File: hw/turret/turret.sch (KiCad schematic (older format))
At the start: 13 parts, among them M1 Motor_Servo wingturn, M2 Motor_Servo wingspan, Q1 MJE3055, SW1 SW_Push, U1 ESP-WROOM-32module, U2 GY291module, U3 AM312module

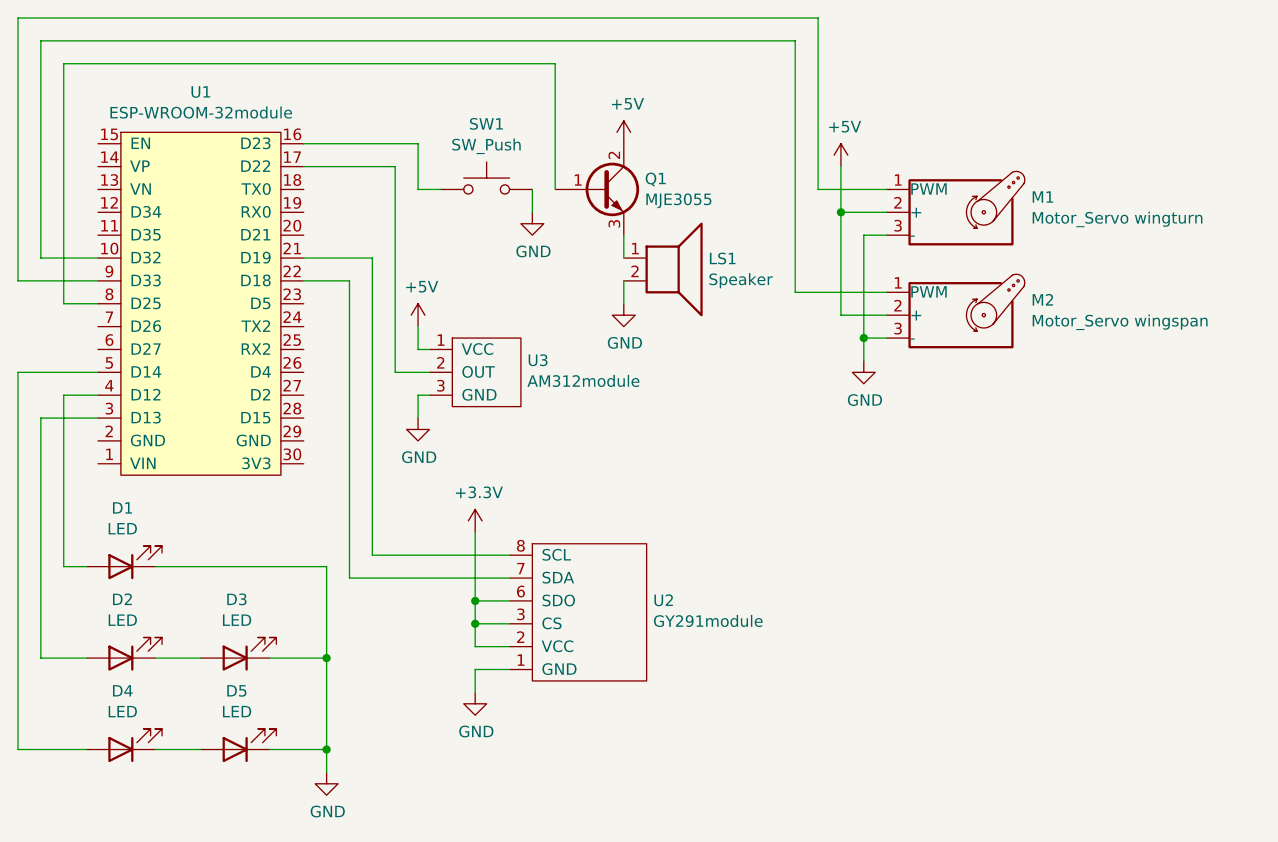
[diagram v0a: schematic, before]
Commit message: hw: adjust schematics for v2 and add PCB
Signed-off-by: Max Filippov <jcmvbkbc@gmail.com>
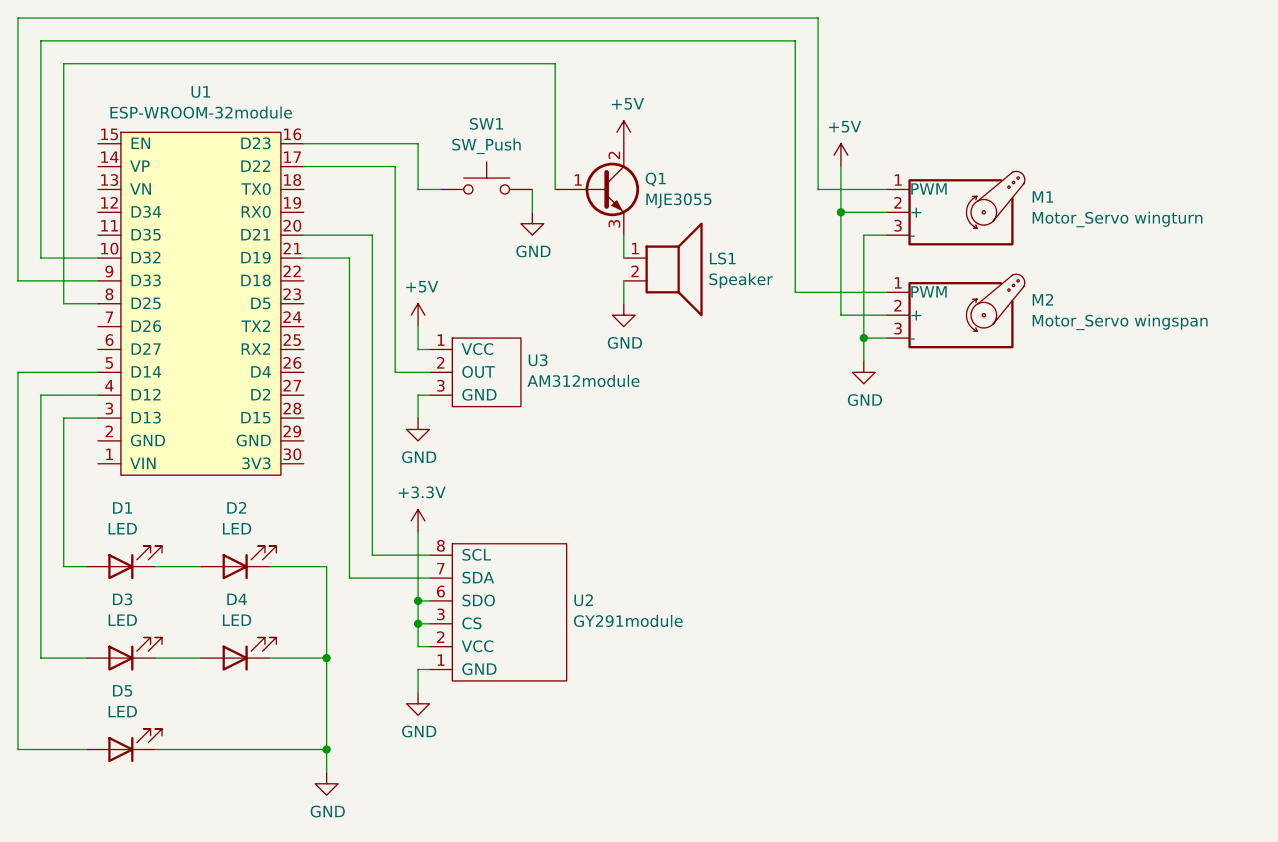
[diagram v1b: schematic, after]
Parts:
- renumbered D2 to D1, D3 to D2, D4 to D3, D5 to D4, D1 to D5
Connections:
- net at U2.7 (SDA): now also U1.21 (D19); no longer U1.22 (D18)
- net at U2.8 (SCL): now also U1.20 (D21); no longer U1.21 (D19)
- net at U1.4 (D12): now also D3.2 (A); no longer D5.2 (A)
- net at U1.5 (D14): now also D5.2 (A); no longer D3.2 (A)
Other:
- moved on the sheet: D1, D2, D3, D4, D5, U2
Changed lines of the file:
@@
 EELAYER 30 0
 EELAYER END
-$Descr A4 11693 8268
+$Descr USLetter 8500 11000 portrait
 encoding utf-8
 Sheet 1 1
-Title ""
-Date ""
-Rev ""
+Title "Portal Turret"
+Date "2023-04-10"
+Rev "v2"
 Comp ""
 Comment1 ""
@@
 Connection ~ 5200 1900
 Wire Wire Line
-	1950 2700 1800 2700
-Wire Wire Line
-	1950 2800 1700 2800
-Wire Wire Line
-	1950 2600 1600 2600
+	1950 2800 1800 2800
 Wire Wire Line
 	1800 2300 1950 2300
@@
 L helpers:GY291module U2
 U 1 1 64208805
-P 4100 3650
-F 0 "U2" H 4378 3701 50  0000 L CNN
-F 1 "GY291module" H 4378 3610 50  0000 L CNN
-F 2 "" H 4100 3700 50  0001 C CNN
-F 3 "" H 4100 3700 50  0001 C CNN
-	1    4100 3650
-	1    0    0    -1
-$EndComp
-Wire Wire Line
-	3050 2200 2850 2200
-Wire Wire Line
-	3150 2100 2850 2100
+P 3750 3650
+F 0 "U2" H 4028 3701 50  0000 L CNN
+F 1 "GY291module" H 4028 3610 50  0000 L CNN
+F 2 "" H 3750 3700 50  0001 C CNN
+F 3 "" H 3750 3700 50  0001 C CNN
+	1    3750 3650
+	1    0    0    -1
+$EndComp
 $Comp
 L power:+3.3V #PWR?
 U 1 1 6420E29C
-P 3600 3300
-F 0 "#PWR?" H 3600 3150 50  0001 C CNN
-F 1 "+3.3V" H 3615 3473 50  0000 C CNN
-F 2 "" H 3600 3300 50  0001 C CNN
-F 3 "" H 3600 3300 50  0001 C CNN
-	1    3600 3300
-	1    0    0    -1
-$EndComp
-Wire Wire Line
-	3750 3800 3600 3800
-Wire Wire Line
-	3600 3800 3600 3700
-Wire Wire Line
-	3750 3700 3600 3700
-Connection ~ 3600 3700
+P 3350 3300
+F 0 "#PWR?" H 3350 3150 50  0001 C CNN
+F 1 "+3.3V" H 3365 3473 50  0000 C CNN
+F 2 "" H 3350 3300 50  0001 C CNN
+F 3 "" H 3350 3300 50  0001 C CNN
+	1    3350 3300
+	1    0    0    -1
+$EndComp
+Wire Wire Line
+	3400 3800 3350 3800
+Wire Wire Line
+	3350 3800 3350 3700
+Wire Wire Line
+	3400 3700 3350 3700
+Connection ~ 3350 3700
 $Comp
 L power:GND #PWR?
 U 1 1 64210F0B
-P 3600 4000
-F 0 "#PWR?" H 3600 3750 50  0001 C CNN
-F 1 "GND" H 3605 3827 50  0000 C CNN
-F 2 "" H 3600 4000 50  0001 C CNN
-F 3 "" H 3600 4000 50  0001 C CNN
-	1    3600 4000
-	1    0    0    -1
-$EndComp
-Wire Wire Line
-	3750 3900 3600 3900
+P 3350 4000
+F 0 "#PWR?" H 3350 3750 50  0001 C CNN
+F 1 "GND" H 3355 3827 50  0000 C CNN
+F 2 "" H 3350 4000 50  0001 C CNN
+F 3 "" H 3350 4000 50  0001 C CNN
+	1    3350 4000
+	1    0    0    -1
+$EndComp
+Wire Wire Line
+	3400 3900 3350 3900
 $Comp
 L helpers:AM312module U3
@@
 	1600 1050 1600 2200
 Wire Wire Line
-	1600 2600 1600 4250
-Wire Wire Line
-	1700 2800 1700 3850
-Wire Wire Line
-	1800 3450 1900 3450
-Wire Wire Line
-	1800 2700 1800 3450
-Wire Wire Line
-	1900 4250 1600 4250
+	1800 2800 1800 3450
 Wire Wire Line
 	1900 3850 1700 3850
 Connection ~ 2950 3850
 Wire Wire Line
+	2950 3450 2700 3450
+Wire Wire Line
 	2950 3850 2950 3450
-Connection ~ 2950 4250
 Wire Wire Line
 	2950 3850 2700 3850
-Wire Wire Line
-	2950 4250 2950 3850
-Wire Wire Line
-	2950 4250 2700 4250
 Wire Wire Line
 	2950 4350 2950 4250
@@
 $EndComp
 Wire Wire Line
-	2200 4250 2400 4250
-Wire Wire Line
 	2200 3850 2400 3850
-$Comp
-L Device:LED D5
+Wire Wire Line
+	2200 3450 2400 3450
+$Comp
+L Device:LED D4
 U 1 1 642176FC
-P 2550 4250
-F 0 "D5" H 2543 3995 50  0000 C CNN
-F 1 "LED" H 2543 4086 50  0000 C CNN
-F 2 "" H 2550 4250 50  0001 C CNN
-F 3 "~" H 2550 4250 50  0001 C CNN
-	1    2550 4250
-	-1   0    0    1
-$EndComp
-$Comp
-L Device:LED D4
-U 1 1 64217295
-P 2050 4250
-F 0 "D4" H 2043 3995 50  0000 C CNN
-F 1 "LED" H 2043 4086 50  0000 C CNN
-F 2 "" H 2050 4250 50  0001 C CNN
-F 3 "~" H 2050 4250 50  0001 C CNN
-	1    2050 4250
-	-1   0    0    1
-$EndComp
-$Comp
-L Device:LED D3
-U 1 1 64216CAC
 P 2550 3850
-F 0 "D3" H 2543 3595 50  0000 C CNN
+F 0 "D4" H 2543 3595 50  0000 C CNN
 F 1 "LED" H 2543 3686 50  0000 C CNN
 F 2 "" H 2550 3850 50  0001 C CNN
@@
 $EndComp
 $Comp
-L Device:LED D2
-U 1 1 64215029
+L Device:LED D3
+U 1 1 64217295
 P 2050 3850
-F 0 "D2" H 2043 3595 50  0000 C CNN
+F 0 "D3" H 2043 3595 50  0000 C CNN
 F 1 "LED" H 2043 3686 50  0000 C CNN
 F 2 "" H 2050 3850 50  0001 C CNN
@@
 $EndComp
 $Comp
+L Device:LED D2
+U 1 1 64216CAC
+P 2550 3450
+F 0 "D2" H 2543 3195 50  0000 C CNN
+F 1 "LED" H 2543 3286 50  0000 C CNN
+F 2 "" H 2550 3450 50  0001 C CNN
+F 3 "~" H 2550 3450 50  0001 C CNN
+	1    2550 3450
+	-1   0    0    1
+$EndComp
+$Comp
 L Device:LED D1
-U 1 1 64212CAF
+U 1 1 64215029
 P 2050 3450
 F 0 "D1" H 2043 3195 50  0000 C CNN
@@
 	-1   0    0    1
 $EndComp
+$Comp
+L Device:LED D5
+U 1 1 64212CAF
+P 2050 4250
+F 0 "D5" H 2043 3995 50  0000 C CNN
+F 1 "LED" H 2043 4086 50  0000 C CNN
+F 2 "" H 2050 4250 50  0001 C CNN
+F 3 "~" H 2050 4250 50  0001 C CNN
+	1    2050 4250
+	-1   0    0    1
+$EndComp
 Wire Wire Line
 	3950 1800 3950 1250
@@
 	1700 2100 1700 1150
 Wire Wire Line
-	3600 3300 3600 3600
-Wire Wire Line
-	3750 3600 3600 3600
-Wire Wire Line
-	3600 3900 3600 4000
-Wire Wire Line
-	2950 3450 2200 3450
-Wire Wire Line
-	3150 2100 3150 3400
-Wire Wire Line
-	3150 3400 3750 3400
-Wire Wire Line
-	3050 2200 3050 3500
-Wire Wire Line
-	3050 3500 3750 3500
-Connection ~ 3600 3600
-Wire Wire Line
-	3600 3600 3600 3700
+	3350 3300 3350 3600
+Wire Wire Line
+	3400 3600 3350 3600
+Wire Wire Line
+	3350 3900 3350 4000
+Wire Wire Line
+	3150 3400 3400 3400
+Wire Wire Line
+	3050 3500 3400 3500
+Connection ~ 3350 3600
+Wire Wire Line
+	3350 3600 3350 3700
+Wire Wire Line
+	2850 2000 3150 2000
+Wire Wire Line
+	3050 2100 2850 2100
+Wire Wire Line
+	3150 2000 3150 3400
+Wire Wire Line
+	3050 2100 3050 3500
+Wire Wire Line
+	1700 2700 1700 3850
+Wire Wire Line
+	1700 2700 1950 2700
+Wire Wire Line
+	1800 3450 1900 3450
+Wire Wire Line
+	1600 2600 1600 4250
+Wire Wire Line
+	1600 4250 1900 4250
+Wire Wire Line
+	1600 2600 1950 2600
+Wire Wire Line
+	2200 4250 2950 4250
+Connection ~ 2950 4250
+Wire Wire Line
+	2950 4250 2950 3850
 $EndSCHEMATC
